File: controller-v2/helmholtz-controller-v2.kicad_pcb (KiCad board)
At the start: 2 copper layers, 36 parts, among them J1 Screw_Terminal_01x02, J2 Screw_Terminal_01x02, J3 Screw_Terminal_01x02, J4 Screw_Terminal_01x02, U1 BDS63150AFM, U2 BDS63150AFM, U3 INA226, U4 INA226, U5 BDS63150AFM, U6 INA226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

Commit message: Updated schematic & board
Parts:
- removed the REF** at (161.2, 55.1)
- removed the REF** at (77.6, 111.2)
- removed the REF** at (161.3, 111.2)
- removed the REF** at (78.0, 54.8)
- added C5: 1uF, Capacitor_SMD:C_0805_2012Metric, F.Cu at (103.1, 69.1)
- added C6: 1uF, Capacitor_SMD:C_0805_2012Metric, F.Cu at (103.4, 80.2)
- added C7: 1uF, Capacitor_SMD:C_0805_2012Metric, F.Cu at (103.0, 96.7)
- added REF**: MountingHole_3.2mm_M3, MountingHole:MountingHole_3.2mm_M3, F.Cu at (139.7, 107.3)
- added REF**: MountingHole_3.2mm_M3, MountingHole:MountingHole_3.2mm_M3, F.Cu at (69.7, 55.6)
- added REF**: MountingHole_3.2mm_M3, MountingHole:MountingHole_3.2mm_M3, F.Cu at (69.4, 107.5)
- added REF**: MountingHole_3.2mm_M3, MountingHole:MountingHole_3.2mm_M3, F.Cu at (139.8, 55.7)
- J1, J2, J3, J4: footprint TerminalBlock_Phoenix:TerminalBlock_Phoenix_PT-1,5-4-3.5-H_1x04_P3.50mm_Horizontal -> TerminalBlock_Phoenix:TerminalBlock_Phoenix_PT-1,5-2-3.5-H_1x02_P3.50mm_Horizontal
- R10, R13, R15, R2, R5, R8: value 0.1Ω -> 100m
- moved R11 64.3 mm to (95.9, 108.9)
- moved R12 60.3 mm to (95.9, 106.9), turned to 180 degrees
- moved R2 37.5 mm to (97.0, 54.2)
- moved R14 34.0 mm to (105.1, 91.4), turned to 180 degrees
- moved R16 32.4 mm to (95.8, 61.9)
- moved C3 31.2 mm to (96.8, 104.6)
- moved U4 29.2 mm to (97.4, 70.1), turned to 180 degrees
- moved C4 29.1 mm to (96.8, 102.3)
- moved R5 26.7 mm to (96.9, 73.2)
- moved U7 26.5 mm to (121.4, 77.4)
- moved U6 25.5 mm to (98.3, 96.1)
- moved R1 25.0 mm to (103.1, 65.3)
- moved C1 24.1 mm to (103.3, 72.5)
- moved C2 23.6 mm to (103.4, 76.4)
- moved R10 23.2 mm to (97.4, 86.8)
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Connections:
- R1 pad 1: Net-(U1-~{FAILA}) -> +3.3V
- R1 pad 2: +3.3V -> Net-(U1-~{FAILA})
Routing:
- net SCL: track 0.00 -> 65.8 mm, vias 0 -> 6
- net SDA: track 0.00 -> 63.0 mm, vias 0 -> 2
- net Net-(J2-Pin_1): track 0.00 -> 52.1 mm, vias 0 -> 8
- net Net-(U5-~{FAILA}): track 0.00 -> 46.8 mm
- net Net-(U3-Vbus): track 0.00 -> 41.7 mm, vias 0 -> 2
- net Net-(J1-Pin_1): track 0.00 -> 37.4 mm
- net Net-(U4-Vbus): track 0.00 -> 26.3 mm
- net Net-(U2-~{FAILA}): track 0.00 -> 22.3 mm, vias 0 -> 2
- net Net-(U6-Vbus): track 0.00 -> 21.5 mm, vias 0 -> 2
- net Net-(U2-RNFS): track 0.00 -> 17.0 mm
- net Net-(U1-~{FAILA}): track 0.00 -> 8.86 mm
- net Net-(U5-RNFS): track 0.00 -> 5.63 mm
- net Net-(U1-RNFS): track 0.00 -> 5.24 mm
- net Net-(J1-Pin_2): track 0.00 -> 4.80 mm
- net Net-(U1-VREF): track 0.00 -> 4.78 mm
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- added copper zone on B.Cu, net GND
- added copper zone on F.Cu, net GND
- removed copper zone on F.Cu, net (none)
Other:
- board outline added: 78.2 x 59.7 mm
- board text added: "Helmholtz Controller Board v2 2025 - 08 - 20"

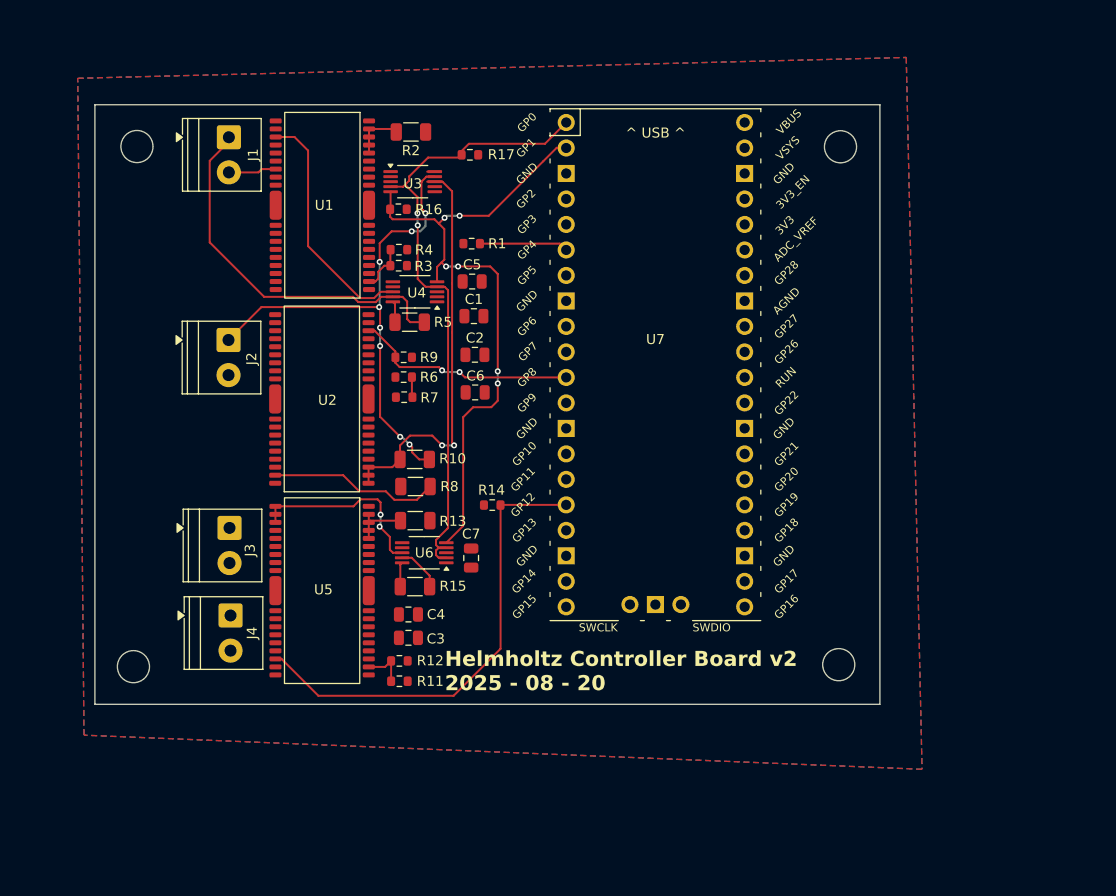
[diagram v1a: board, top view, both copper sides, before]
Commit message: Indicators & test points added
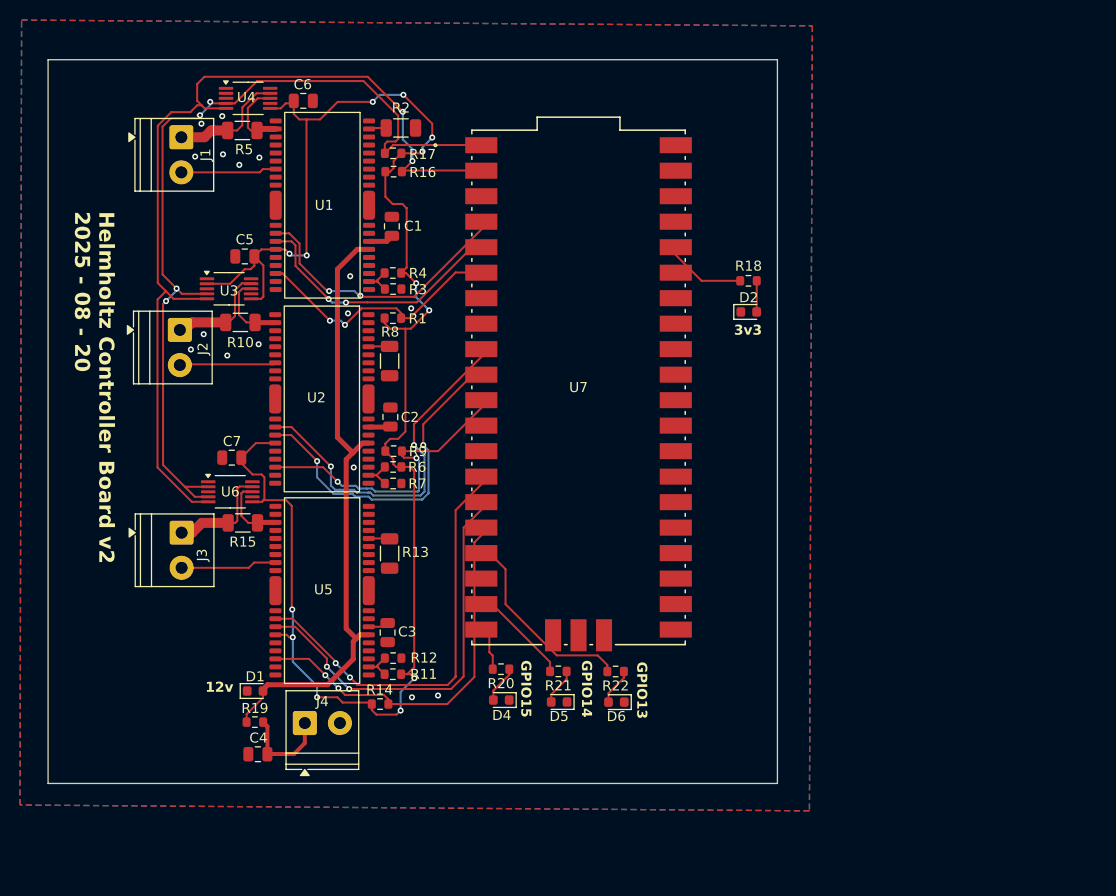
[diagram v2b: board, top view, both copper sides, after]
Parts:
- removed REF** (x4): MountingHole_3.2mm_M3, MountingHole:MountingHole_3.2mm_M3
- added D1: LED, LED_SMD:LED_0603_1608Metric, F.Cu at (81.5, 109.9)
- added D2: LED, LED_SMD:LED_0603_1608Metric, F.Cu at (130.7, 72.1)
- added D4: LED, LED_SMD:LED_0603_1608Metric, F.Cu at (106.0, 110.8)
- added D5: LED, LED_SMD:LED_0603_1608Metric, F.Cu at (111.8, 111.0)
- added D6: LED, LED_SMD:LED_0603_1608Metric, F.Cu at (117.5, 111.0)
- added R18: 660, Resistor_SMD:R_0603_1608Metric, F.Cu at (130.7, 69.0)
- added R19: 2.4k, Resistor_SMD:R_0603_1608Metric, F.Cu at (81.5, 113.0)
- added R20: 660, Resistor_SMD:R_0603_1608Metric, F.Cu at (106.0, 107.7)
- added R21: 660, Resistor_SMD:R_0603_1608Metric, F.Cu at (111.7, 107.9)
- added R22: 660, Resistor_SMD:R_0603_1608Metric, F.Cu at (117.4, 108.0)
- U7: footprint oresat-misc:RPi_Pico_TH -> oresat-misc:RPi_Pico_Castellated
- moved C6 33.7 mm to (86.3, 51.1), turned to 180 degrees
- moved C7 25.9 mm to (79.2, 86.7), turned to 0 degrees
- moved U4 25.5 mm to (80.8, 50.9), turned to 0 degrees
- moved R5 25.4 mm to (80.2, 54.0), turned to 180 degrees
- moved C5 22.8 mm to (80.5, 66.6)
- moved R14 22.8 mm to (94.0, 111.2)
- moved R10 22.1 mm to (80.0, 73.2), turned to 180 degrees
- moved U3 21.2 mm to (78.9, 69.8)
- moved C4 20.5 mm to (81.8, 116.2)
- moved U6 20.3 mm to (79.0, 90.0), turned to 0 degrees
- moved R15 18.3 mm to (80.3, 93.2), turned to 180 degrees
- moved J4 13.0 mm to (86.5, 113.1), turned to 0 degrees
- moved R8 12.8 mm to (94.9, 77.0), turned to -90 degrees
- moved C1 12.1 mm to (95.1, 63.6), turned to -90 degrees
- moved R1 10.8 mm to (95.2, 72.8)
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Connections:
- net +5V renamed +5.0V
- U7 pad 17: unconnected-(U7-GPIO13-Pad17) -> Net-(U7-GPIO13)
- U7 pad 19: unconnected-(U7-GPIO14-Pad19) -> Net-(U7-GPIO14)
- U7 pad 20: unconnected-(U7-GPIO15-Pad20) -> Net-(U7-GPIO15)
- U7 pad 36: +3.3V -> Net-(U7-3V3)
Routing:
- net +3.3V: track 0.00 -> 171.4 mm, vias 0 -> 13
- net +12V: track 0.00 -> 74.3 mm
- net Net-(U5-IN1): track 0.00 -> 42.6 mm, vias 0 -> 2
- net Net-(U5-IN2): track 0.00 -> 40.8 mm, vias 0 -> 2
- net Net-(J2-Pin_1): track 52.1 -> 11.4 mm, vias 8 -> 0
- net Net-(U2-IN1): track 0.00 -> 36.7 mm, vias 0 -> 2
- net Net-(U2-IN2): track 0.00 -> 35.0 mm, vias 0 -> 2
- net Net-(U3-Vbus): track 41.7 -> 7.88 mm, vias 2 -> 0
- net Net-(U1-IN1): track 0.00 -> 28.2 mm, vias 0 -> 2
- net SCL: track 65.8 -> 93.5 mm, vias 6 -> 2
- net Net-(U1-IN2): track 0.00 -> 27.3 mm, vias 0 -> 2
- net SDA: track 63.0 -> 89.2 mm, vias 2 -> 4
- net Net-(J1-Pin_1): track 37.4 -> 11.7 mm
- net Net-(U7-GPIO13): track 0.00 -> 19.1 mm
- net Net-(U4-Vbus): track 26.3 -> 7.75 mm
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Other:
- board size 78.2 x 59.7 mm -> 72.7 x 72.1 mm
- board text added: "12v"
- board text added: "3v3"
- board text added: "GPIO13"
- board text added: "GPIO14"
- board text added: "GPIO15"

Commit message: Pre-final review
UART still needs to be connected
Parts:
- added J5: Conn_01x04, Connector_PinHeader_2.54mm:PinHeader_1x04_P2.54mm_Vertical, F.Cu at (128.6, 71.8)
- added TP1: Test-Point, oresat-misc:TestPoint-0.75mm-th, F.Cu at (80.8, 103.8)
- added TP2: Test-Point, oresat-misc:TestPoint-0.75mm-th, F.Cu at (78.3, 102.3)
- added TP3: Test-Point, oresat-misc:TestPoint-0.75mm-th, F.Cu at (81.0, 82.8)
- added TP4: Test-Point, oresat-misc:TestPoint-0.75mm-th, F.Cu at (78.2, 82.8)
- added TP5: Test-Point, oresat-misc:TestPoint-0.75mm-th, F.Cu at (81.0, 63.1)
- added TP6: Test-Point, oresat-misc:TestPoint-0.75mm-th, F.Cu at (78.2, 63.1)
- added TP7: Test-Point, oresat-misc:TestPoint-0.75mm-th, F.Cu at (98.6, 61.5)
- added TP8: Test-Point, oresat-misc:TestPoint-0.75mm-th, F.Cu at (98.5, 50.2)
- moved R18 8.94 mm to (128.5, 60.4)
- moved D2 8.94 mm to (128.6, 63.5)
- moved U7 5.31 mm to (114.1, 74.3)
- moved D5 4.71 mm to (112.0, 106.3)
- moved D4 4.71 mm to (106.2, 106.1)
- moved D6 4.71 mm to (117.7, 106.3)
- moved R20 4.71 mm to (106.2, 103.0)
- moved R21 4.71 mm to (111.9, 103.2)
- moved R22 4.71 mm to (117.6, 103.2)
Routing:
- net GND: track 0.02 -> 15.1 mm, vias 16 -> 29
- net Net-(U2-IN2): track 35.0 -> 47.5 mm
- net Net-(U5-IN1): track 42.6 -> 53.8 mm
- net Net-(U1-IN2): track 27.3 -> 38.2 mm
- net Net-(U1-IN1): track 28.2 -> 37.8 mm
- net Net-(U2-IN1): track 36.7 -> 46.3 mm
- net Net-(U5-IN2): track 40.8 -> 49.6 mm
- net Net-(U5-~{FAILA}): track 38.6 -> 44.4 mm
- net Net-(U2-~{FAILA}): track 31.5 -> 37.1 mm
- net SDA: track 89.2 -> 94.8 mm
- net SCL: track 93.5 -> 98.7 mm
- net Net-(U7-GPIO13): track 19.1 -> 24.3 mm
- net Net-(U7-3V3): track 8.72 -> 3.96 mm
- net Net-(U1-~{FAILA}): track 26.4 -> 30.9 mm
- net Net-(U7-GPIO14): track 9.38 -> 12.2 mm
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
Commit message: Pre-final Review
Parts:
- moved J5 21.9 mm to (129.6, 93.7)
- moved J3 0.83 mm to (73.3, 94.2)
- moved R15 0.75 mm to (79.5, 93.1)
- moved J2 0.68 mm to (73.3, 73.7)
- moved R13 0.65 mm to (95.5, 96.2)
- moved C3 0.45 mm to (94.9, 103.7)
- moved R12 0.37 mm to (95.4, 106.3)
- moved R10 0.29 mm to (79.8, 73.2)
- moved R7 0.23 mm to (95.5, 89.2)
- moved R11 0.22 mm to (95.4, 108.1)
- moved R6 0.20 mm to (95.5, 87.6)
- moved R9 0.15 mm to (95.5, 86.0)
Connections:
- J5 pad 1: unconnected-(J5-Pin_1-Pad1) -> +3.3V
- J5 pad 2: unconnected-(J5-Pin_2-Pad2) -> Net-(J5-Pin_2)
- J5 pad 3: unconnected-(J5-Pin_3-Pad3) -> Net-(J5-Pin_3)
- J5 pad 4: unconnected-(J5-Pin_4-Pad4) -> GND
- R18 pad 2: Net-(U7-3V3) -> +3.3V
- U7 pad 13: unconnected-(U7-GND-Pad13) -> GND
- U7 pad 18: unconnected-(U7-GND-Pad18) -> GND
- U7 pad 21: unconnected-(U7-GPIO16-Pad21) -> Net-(J5-Pin_3)
- U7 pad 22: unconnected-(U7-GPIO17-Pad22) -> Net-(J5-Pin_2)
- U7 pad 28: unconnected-(U7-GND-Pad28) -> GND
- U7 pad 3: unconnected-(U7-GND-Pad3) -> GND
- U7 pad 33: unconnected-(U7-AGND-Pad33) -> GND
- U7 pad 36: Net-(U7-3V3) -> +3.3V
- U7 pad 38: unconnected-(U7-GND-Pad38) -> GND
- U7 pad 8: unconnected-(U7-GND-Pad8) -> GND
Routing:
- net +3.3V: track 173.9 -> 273.1 mm, vias 13 -> 16
- net GND: track 15.1 -> 2.81 mm, vias 29 -> 77
- net Net-(J5-Pin_2): track 0.00 -> 5.97 mm
- net Net-(J5-Pin_3): track 0.00 -> 5.97 mm
- net Net-(U6-Vbus): track 7.40 -> 12.4 mm
- net Net-(U3-Vbus): track 7.88 -> 12.8 mm
- net +12V: track 76.6 -> 81.4 mm
- net Net-(U4-Vbus): track 7.75 -> 12.5 mm
- net Net-(U7-3V3): track 3.96 -> 0.00 mm
- net Net-(U1-RNFS): track 2.15 -> 4.62 mm
- net Net-(U5-RNFS): track 1.89 -> 4.29 mm
- net Net-(U2-RNFS): track 1.84 -> 4.24 mm
- net Net-(J1-Pin_2): track 9.53 -> 11.1 mm
- net Net-(J2-Pin_2): track 9.92 -> 11.5 mm
- net Net-(J3-Pin_2): track 9.57 -> 11.2 mm
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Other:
- board text added: "Helmholtz Controller Board v2 2025 - 08 - 26"
- board text added: "Shaelin Olton"
- board text removed: "Helmholtz Controller Board v2 2025 - 08 - 20"

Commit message: Final Review Ready
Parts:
- added REF**: MountingHole_3.2mm_M3, MountingHole:MountingHole_3.2mm_M3, F.Cu at (129.3, 114.8)
- added REF**: MountingHole_3.2mm_M3, MountingHole:MountingHole_3.2mm_M3, F.Cu at (129.5, 51.3)
- added REF**: MountingHole_3.2mm_M3, MountingHole:MountingHole_3.2mm_M3, F.Cu at (65.2, 51.2)
- added REF**: MountingHole_3.2mm_M3, MountingHole:MountingHole_3.2mm_M3, F.Cu at (65.4, 114.8)
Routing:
- net +3.3V: track 273.1 -> 267.9 mm

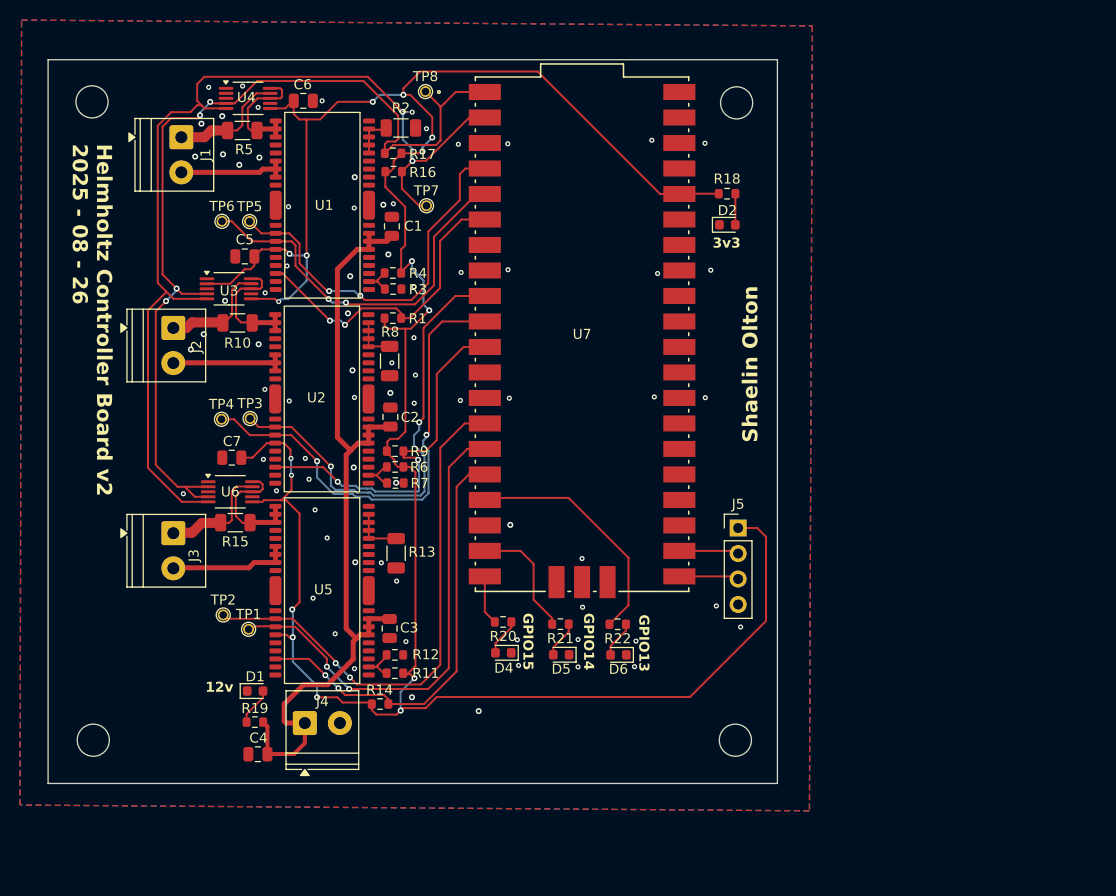
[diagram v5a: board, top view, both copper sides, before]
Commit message: Fix BD IC symbols, fix some ERCs, put mounting holes in the schematic.
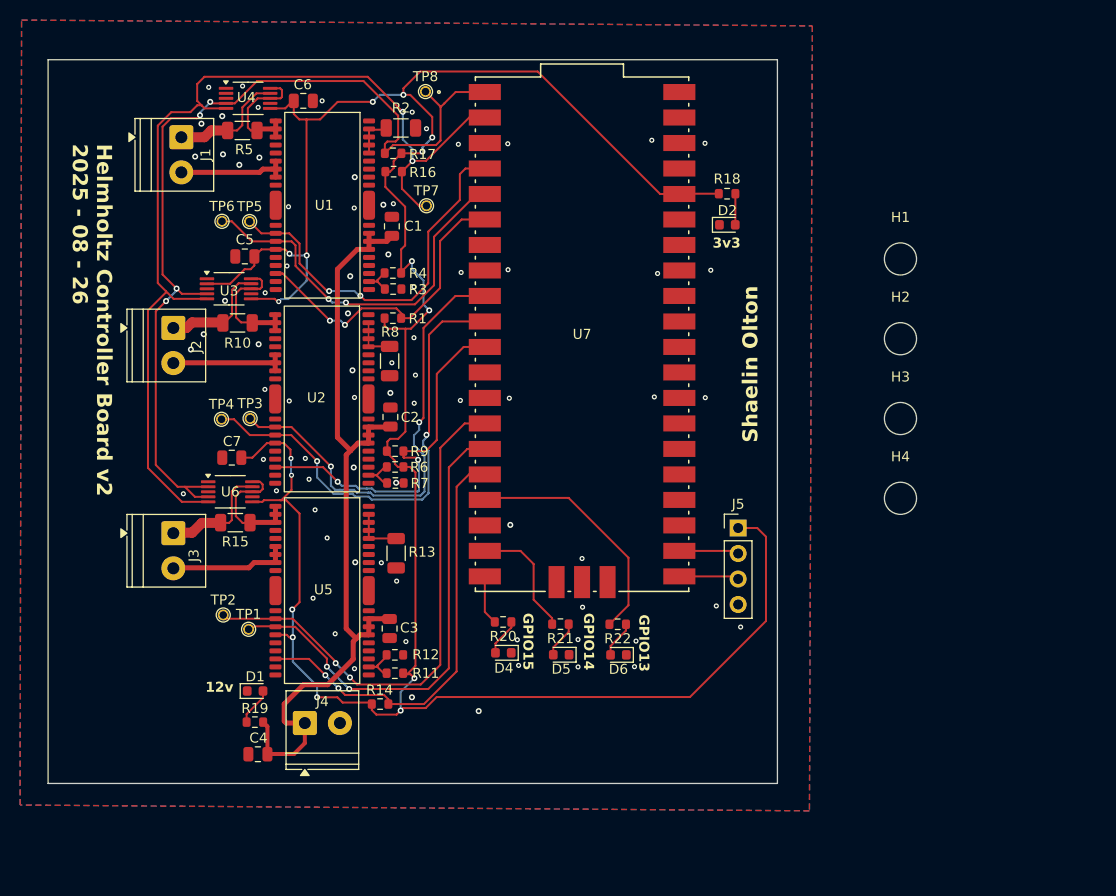
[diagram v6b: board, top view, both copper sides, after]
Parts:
- removed REF** (x4): MountingHole_3.2mm_M3, MountingHole:MountingHole_3.2mm_M3
- added H1: MountingHole, MountingHole:MountingHole_3.2mm_M3, F.Cu at (145.8, 66.8)
- added H2: MountingHole, MountingHole:MountingHole_3.2mm_M3, F.Cu at (145.8, 74.8)
- added H3: MountingHole, MountingHole:MountingHole_3.2mm_M3, F.Cu at (145.8, 82.8)
- added H4: MountingHole, MountingHole:MountingHole_3.2mm_M3, F.Cu at (145.8, 90.7)
- D1, D2, D5: value LED -> GRN
- D4: value LED -> BLU
- D6: value LED -> RED
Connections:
- U1 pad 10: (no net) -> unconnected-(U1-NC-Pad10)
- U1 pad 14: (no net) -> unconnected-(U1-NC-Pad14)
- U1 pad 17: (no net) -> unconnected-(U1-NC-Pad17)
- U1 pad 19: (no net) -> unconnected-(U1-NC-Pad19)
- U1 pad 21: (no net) -> unconnected-(U1-NC-Pad21)
- U1 pad 22: (no net) -> GND
- U1 pad 23: (no net) -> unconnected-(U1-NC-Pad23)
- U1 pad 27: (no net) -> unconnected-(U1-NC-Pad27)
- U1 pad 28: (no net) -> unconnected-(U1-NC-Pad28)
- U1 pad 30: (no net) -> unconnected-(U1-NC-Pad30)
- U1 pad 31: (no net) -> unconnected-(U1-NC-Pad31)
- U1 pad 36: (no net) -> unconnected-(U1-NC-Pad36)
- U1 pad 4: (no net) -> unconnected-(U1-NC-Pad4)
- U1 pad 5: (no net) -> unconnected-(U1-NC-Pad5)
- U1 pad 9: (no net) -> unconnected-(U1-NC-Pad9)
- U1 pad FIN: GND -> (no net)
- U2 pad 10: (no net) -> unconnected-(U2-NC-Pad10)
- U2 pad 14: (no net) -> unconnected-(U2-NC-Pad14)
- U2 pad 17: (no net) -> unconnected-(U2-NC-Pad17)
- U2 pad 19: (no net) -> unconnected-(U2-NC-Pad19)
- U2 pad 21: (no net) -> unconnected-(U2-NC-Pad21)
- U2 pad 22: (no net) -> GND
- U2 pad 23: (no net) -> unconnected-(U2-NC-Pad23)
- U2 pad 27: (no net) -> unconnected-(U2-NC-Pad27)
- U2 pad 28: (no net) -> unconnected-(U2-NC-Pad28)
- U2 pad 30: (no net) -> unconnected-(U2-NC-Pad30)
- U2 pad 31: (no net) -> unconnected-(U2-NC-Pad31)
- U2 pad 36: (no net) -> unconnected-(U2-NC-Pad36)
- U2 pad 4: (no net) -> unconnected-(U2-NC-Pad4)
- U2 pad 5: (no net) -> unconnected-(U2-NC-Pad5)
- U2 pad 9: (no net) -> unconnected-(U2-NC-Pad9)
- U2 pad FIN: GND -> (no net)
- U5 pad 10: (no net) -> unconnected-(U5-NC-Pad10)
- U5 pad 14: (no net) -> unconnected-(U5-NC-Pad14)
- U5 pad 17: (no net) -> unconnected-(U5-NC-Pad17)
- U5 pad 19: (no net) -> unconnected-(U5-NC-Pad19)
- U5 pad 21: (no net) -> unconnected-(U5-NC-Pad21)
- U5 pad 22: (no net) -> GND
- U5 pad 23: (no net) -> unconnected-(U5-NC-Pad23)
- U5 pad 27: (no net) -> unconnected-(U5-NC-Pad27)
- U5 pad 28: (no net) -> unconnected-(U5-NC-Pad28)
- U5 pad 30: (no net) -> unconnected-(U5-NC-Pad30)
- U5 pad 31: (no net) -> unconnected-(U5-NC-Pad31)
- U5 pad 36: (no net) -> unconnected-(U5-NC-Pad36)
- U5 pad 4: (no net) -> unconnected-(U5-NC-Pad4)
- U5 pad 5: (no net) -> unconnected-(U5-NC-Pad5)
- U5 pad 9: (no net) -> unconnected-(U5-NC-Pad9)
- U5 pad FIN: GND -> (no net)
- U7 pad 23: unconnected-(U7-GND-Pad23) -> GND
